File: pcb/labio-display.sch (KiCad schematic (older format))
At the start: 6 parts, among them P401 SFV12R-1ST__HLF, SW401 DIP_SWITCH_X04, U401 CFAL12832D-B

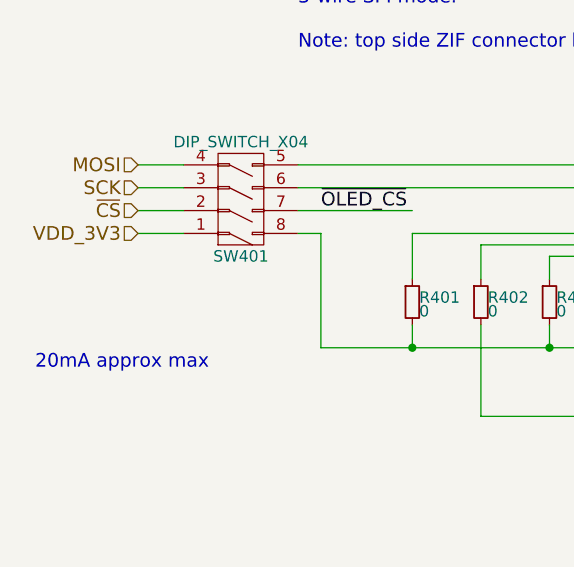
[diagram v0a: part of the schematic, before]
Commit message: Fix ADC reading mic, possible backpowering, encoder pull downs, vias in footprint:
* Mic needs on-board path to ADC. Add proper bias and amp. Connect to ADC or codec with switches.
* Mic footprint (U701) flipped. Redraw footprint and adjust routing.
* Remove power from dip switches and replace with fuses. Turning power off to a block could result in backpower from driven IO lines.
* Remove/adjust pull downs on LEDs for encoder/dpad lines.
* Move vias out of display connector (P401) footprint.
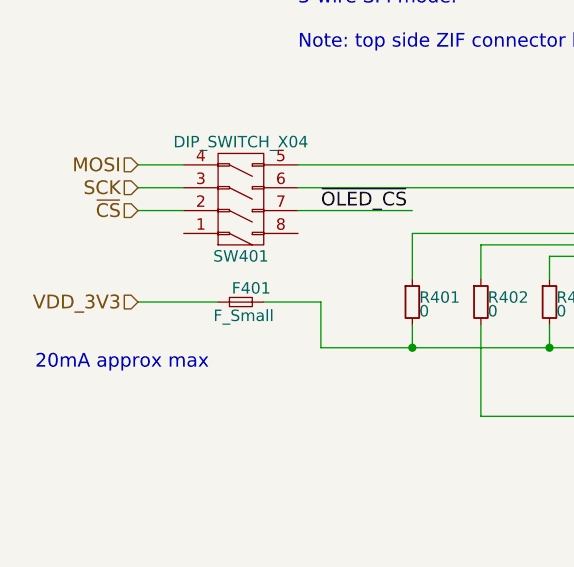
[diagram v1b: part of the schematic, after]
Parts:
- added F401: F_Small, Resistors_SMD:R_1206, symbol F_Small
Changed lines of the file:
@@
 encoding utf-8
 Sheet 4 10
-Title ""
+Title "Raspberry Pi Embedded Lab I/O"
 Date ""
-Rev ""
-Comp ""
+Rev "1.1.4"
+Comp "Carnegie Mellon University"
 Comment1 ""
-Comment2 ""
+Comment2 "Drawn by: Ian Hartwig"
 Comment3 ""
 Comment4 ""
@@
 	6000 2400 6600 2400
 Connection ~ 6000 3500
-Text HLabel 3800 2900 0    60   Input ~ 0
+Text HLabel 3800 3200 0    60   Input ~ 0
 VDD_3V3
 Text HLabel 3800 2800 0    60   Input ~ 0
@@
 03 00 00 00 00 F4 24 84 F2 00 00 00 00 00 3D 09 A1 3C 00 00 00 00 40 4F 42 28 0F 00 00 00 00 D0
 93 10 CA 03 00 00 00 00 F4 24 84 F2 00 00 00 00 00 3D 09 A1 3C 00 00 00 00 40 4F FA 3F 4E 16 A4
-A2 80 4C E9 AA 00 00 00 00 49 45 4E 44 AE 42 60 82 00
+A2 80 4C E9 AA 00 00 00 00 49 45 4E 44 AE 42 60 82 3B
 EndData
 $EndBitmap
@@
 $EndComp
 Wire Wire Line
-	3800 2900 4000 2900
-Wire Wire Line
 	4000 2600 3800 2600
 Wire Wire Line
@@
 	4600 3400 6600 3400
 Wire Wire Line
-	4600 3400 4600 2900
-Wire Wire Line
-	4600 2900 4500 2900
-Wire Wire Line
 	6600 3300 6100 3300
 Wire Wire Line
@@
 	1    0    0    -1
 $EndComp
+$Comp
+L F_Small F401
+U 1 1 57AFAD90
+P 4250 3200
+F 0 "F401" H 4210 3260 50  0000 L CNN
+F 1 "F_Small" H 4130 3140 50  0000 L CNN
+F 2 "Resistors_SMD:R_1206" H 4250 3200 50  0001 C CNN
+F 3 "" H 4250 3200 50  0000 C CNN
+	1    4250 3200
+	1    0    0    -1
+$EndComp
+Wire Wire Line
+	4350 3200 4600 3200
+Wire Wire Line
+	4600 3200 4600 3400
+Wire Wire Line
+	3800 3200 4150 3200
 $EndSCHEMATC

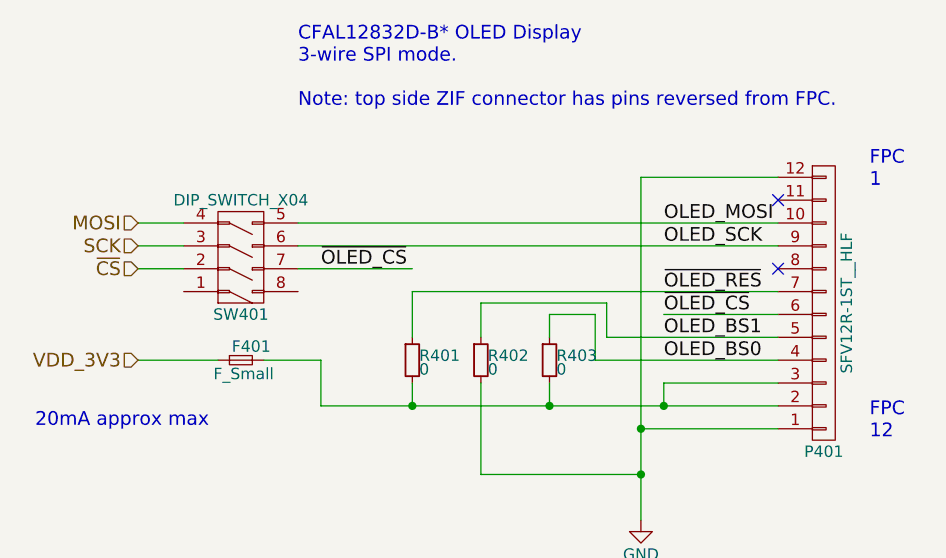
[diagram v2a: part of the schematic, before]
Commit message: using MISO/gpio for D/C on led screen and layout. bump to rev 1.2.0.
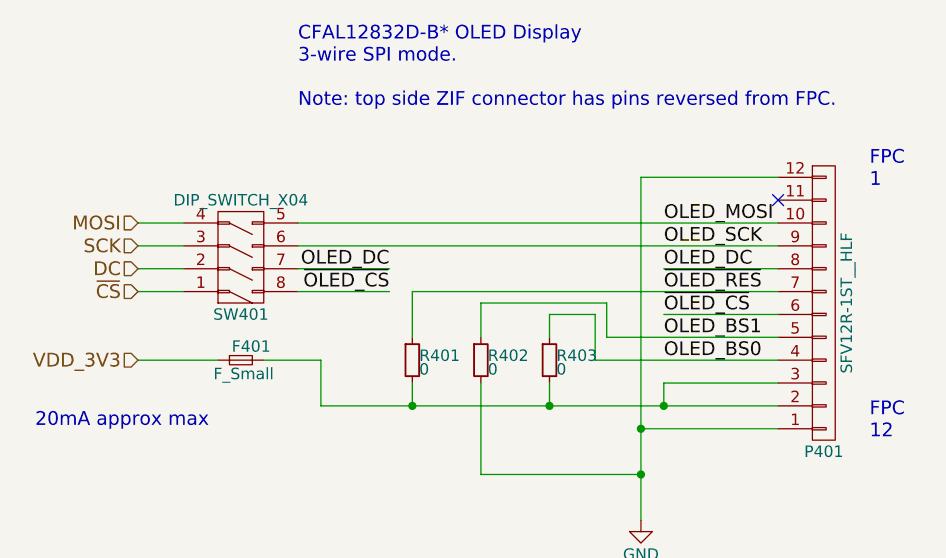
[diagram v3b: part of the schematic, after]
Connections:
- net labels added: DC, OLED_DC
- wire segments 30 -> 33
- no-connect marks 2 -> 1
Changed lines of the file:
@@
 Title "Raspberry Pi Embedded Lab I/O"
 Date ""
-Rev "1.1.4"
+Rev "1.2.0"
 Comp "Carnegie Mellon University"
 Comment1 ""
@@
 Text HLabel 3800 3200 0    60   Input ~ 0
 VDD_3V3
-Text HLabel 3800 2800 0    60   Input ~ 0
+Text HLabel 3800 2900 0    60   Input ~ 0
 ~CS
-NoConn ~ 6600 2800
 Text HLabel 3800 2700 0    60   Input ~ 0
 SCK
@@
 03 00 00 00 00 F4 24 84 F2 00 00 00 00 00 3D 09 A1 3C 00 00 00 00 40 4F 42 28 0F 00 00 00 00 D0
 93 10 CA 03 00 00 00 00 F4 24 84 F2 00 00 00 00 00 3D 09 A1 3C 00 00 00 00 40 4F FA 3F 4E 16 A4
-A2 80 4C E9 AA 00 00 00 00 49 45 4E 44 AE 42 60 82 A3
+A2 80 4C E9 AA 00 00 00 00 49 45 4E 44 AE 42 60 82 FF
 EndData
 $EndBitmap
@@
 Text Label 6100 3000 0    60   ~ 0
 ~OLED_CS
-Text Label 4600 2800 0    60   ~ 0
+Text Label 4900 2900 2    60   ~ 0
 ~OLED_CS
 Wire Wire Line
-	4500 2800 5000 2800
+	4500 2800 4900 2800
 Text Label 6100 2700 0    60   ~ 0
 OLED_SCK
@@
 Wire Wire Line
 	3800 3200 4150 3200
+Wire Wire Line
+	6600 2800 6100 2800
+Text Label 6100 2800 0    60   ~ 0
+OLED_DC
+Wire Wire Line
+	4500 2900 4900 2900
+Text Label 4900 2800 2    60   ~ 0
+OLED_DC
+Text HLabel 3800 2800 0    60   Input ~ 0
+DC
+Wire Wire Line
+	3800 2900 4000 2900
 $EndSCHEMATC

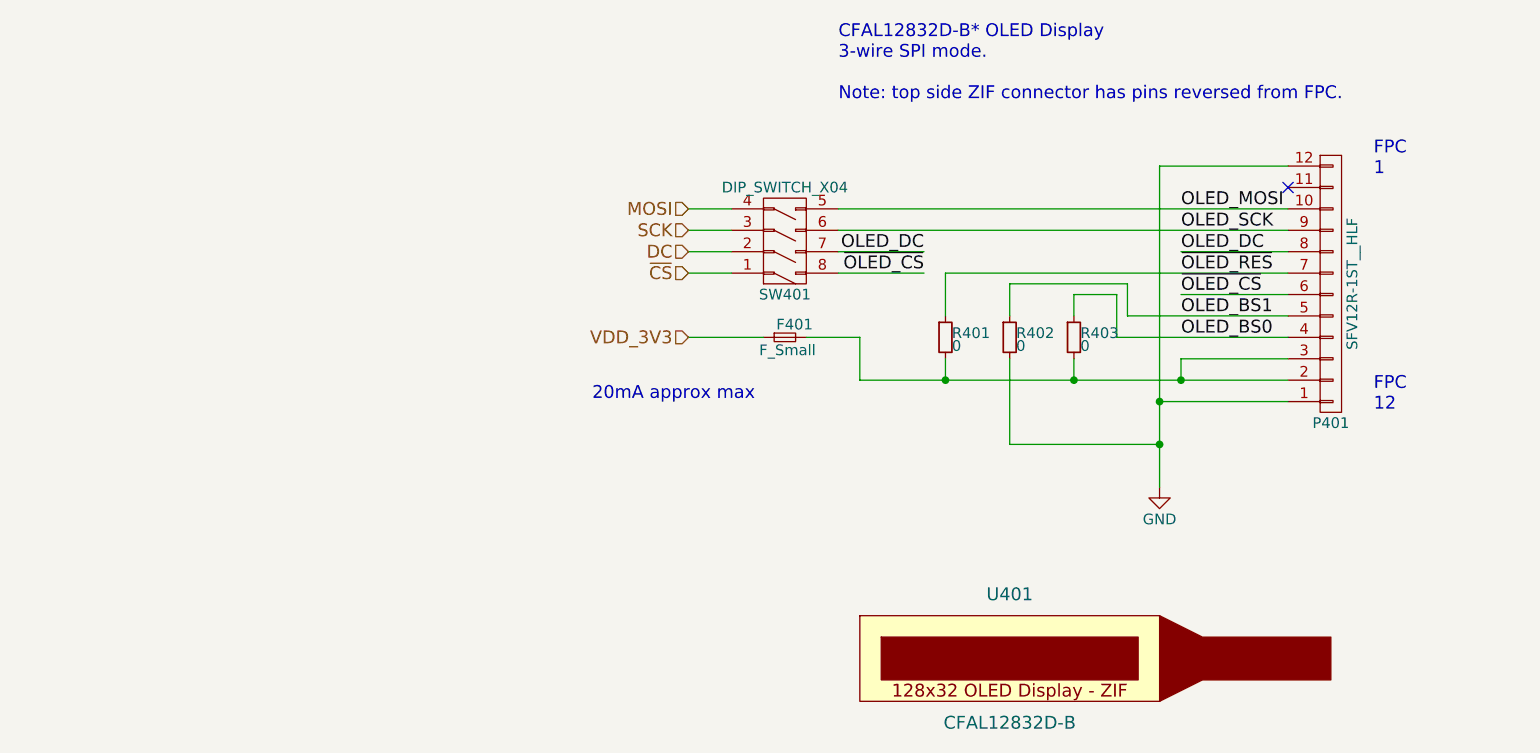
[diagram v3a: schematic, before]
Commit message: add options for driving oled reset. no changes to stuffed bom parts.
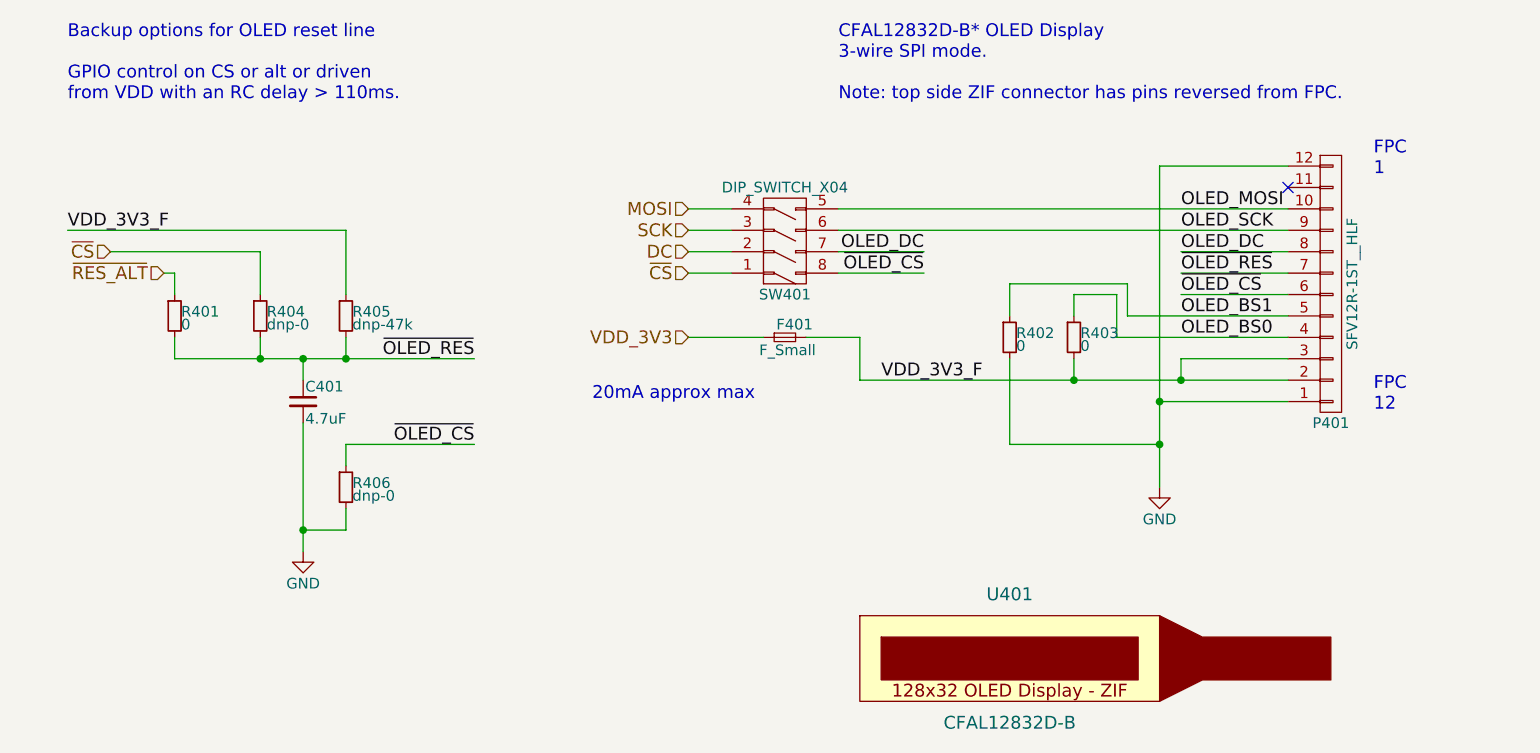
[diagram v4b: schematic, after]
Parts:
- added C401: 4.7uF, Capacitors_SMD:C_0805, symbol C_Small
- added R401: 0, Resistors_SMD:R_0603, symbol R_Small
- added R404, R406: dnp-0, Resistors_SMD:R_0603, symbol R_Small
- R405: renamed from R401; value 0 -> dnp-47k
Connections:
- net GND: now also C401.2, R406.2
- net ~CS: now also R404.1
- net ~OLED_CS: now also R406.1
- net ~OLED_RES: now also R405.2, C401.1, R401.2, R404.2; no longer R405.1
- net VDD_3V3_F: now reaches F401.2, P401.2 (P2), P401.3 (P3), R403.2
- net VDD_3V3_F: now also R405.1; no longer R405.2
- new net ~RES_ALT: R401.1
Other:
- note added: "Backup options for OLED reset line\n\nGPIO control on CS or alt or driven\nfrom VDD with an RC delay > 110ms."
- moved on the sheet: R405
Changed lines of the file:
@@
 20mA approx max
 $Comp
-L R_Small R401
+L R_Small R405
 U 1 1 5766D812
-P 5000 3200
-F 0 "R401" H 5030 3220 50  0000 L CNN
-F 1 "0" H 5030 3160 50  0000 L CNN
-F 2 "Resistors_SMD:R_0603" H 5000 3200 50  0001 C CNN
-F 3 "" H 5000 3200 50  0000 C CNN
-	1    5000 3200
+P 2200 3100
+F 0 "R405" H 2230 3120 50  0000 L CNN
+F 1 "dnp-47k" H 2230 3060 50  0000 L CNN
+F 2 "Resistors_SMD:R_0603" H 2200 3100 50  0001 C CNN
+F 3 "" H 2200 3100 50  0000 C CNN
+	1    2200 3100
 	1    0    0    -1
 $EndComp
@@
 	5600 3300 5600 3400
 Connection ~ 5600 3400
-Wire Wire Line
-	5000 3300 5000 3400
-Connection ~ 5000 3400
-Wire Wire Line
-	6600 2900 5000 2900
-Wire Wire Line
-	5000 2900 5000 3100
 $Comp
 L R_Small R402
@@
 Wire Wire Line
 	3800 2900 4000 2900
+$Comp
+L C_Small C401
+U 1 1 57BD0C4A
+P 2000 3500
+F 0 "C401" H 2010 3570 50  0000 L CNN
+F 1 "4.7uF" H 2010 3420 50  0000 L CNN
+F 2 "Capacitors_SMD:C_0805" H 2000 3500 50  0001 C CNN
+F 3 "" H 2000 3500 50  0000 C CNN
+	1    2000 3500
+	1    0    0    -1
+$EndComp
+$Comp
+L R_Small R404
+U 1 1 57BD0DE0
+P 1800 3100
+F 0 "R404" H 1830 3120 50  0000 L CNN
+F 1 "dnp-0" H 1830 3060 50  0000 L CNN
+F 2 "Resistors_SMD:R_0603" H 1800 3100 50  0001 C CNN
+F 3 "" H 1800 3100 50  0000 C CNN
+	1    1800 3100
+	1    0    0    -1
+$EndComp
+$Comp
+L R_Small R401
+U 1 1 57BD0E72
+P 1400 3100
+F 0 "R401" H 1430 3120 50  0000 L CNN
+F 1 "0" H 1430 3060 50  0000 L CNN
+F 2 "Resistors_SMD:R_0603" H 1400 3100 50  0001 C CNN
+F 3 "" H 1400 3100 50  0000 C CNN
+	1    1400 3100
+	1    0    0    -1
+$EndComp
+$Comp
+L R_Small R406
+U 1 1 57BD0EA6
+P 2200 3900
+F 0 "R406" H 2230 3920 50  0000 L CNN
+F 1 "dnp-0" H 2230 3860 50  0000 L CNN
+F 2 "Resistors_SMD:R_0603" H 2200 3900 50  0001 C CNN
+F 3 "" H 2200 3900 50  0000 C CNN
+	1    2200 3900
+	1    0    0    -1
+$EndComp
+Wire Wire Line
+	6600 2900 6100 2900
+Wire Wire Line
+	1400 3000 1400 2900
+Wire Wire Line
+	1400 2900 1350 2900
+$Comp
+L GND #PWR010
+U 1 1 57BD11F8
+P 2000 4200
+F 0 "#PWR010" H 2000 3950 50  0001 C CNN
+F 1 "GND" H 2000 4050 50  0000 C CNN
+F 2 "" H 2000 4200 50  0000 C CNN
+F 3 "" H 2000 4200 50  0000 C CNN
+	1    2000 4200
+	1    0    0    -1
+$EndComp
+Wire Wire Line
+	2000 4200 2000 3600
+Wire Wire Line
+	1400 3200 1400 3300
+Wire Wire Line
+	1400 3300 2800 3300
+Wire Wire Line
+	2000 3300 2000 3400
+Wire Wire Line
+	1800 3300 1800 3200
+Connection ~ 1800 3300
+Connection ~ 2000 3300
+Wire Wire Line
+	2200 3200 2200 3300
+Connection ~ 2200 3300
+Wire Wire Line
+	1800 3000 1800 2800
+Wire Wire Line
+	1800 2800 1100 2800
+Wire Wire Line
+	2200 3000 2200 2700
+Wire Wire Line
+	2200 2700 900  2700
+Text Label 4700 3400 0    60   ~ 0
+VDD_3V3_F
+Text Label 900  2700 0    60   ~ 0
+VDD_3V3_F
+Text Label 2800 3300 2    60   ~ 0
+~OLED_RES
+Wire Wire Line
+	2200 3700 2800 3700
+Text Label 2800 3700 2    60   ~ 0
+~OLED_CS
+Text HLabel 1100 2800 0    60   Input ~ 0
+~CS
+Text HLabel 1350 2900 0    60   Input ~ 0
+~RES_ALT
+Wire Wire Line
+	2200 3700 2200 3800
+Wire Wire Line
+	2200 4000 2200 4100
+Wire Wire Line
+	2200 4100 2000 4100
+Connection ~ 2000 4100
+Text Notes 900  2100 0    60   ~ 0
+Backup options for OLED reset line\n\nGPIO control on CS or alt or driven\nfrom VDD with an RC delay > 110ms.
 $EndSCHEMATC

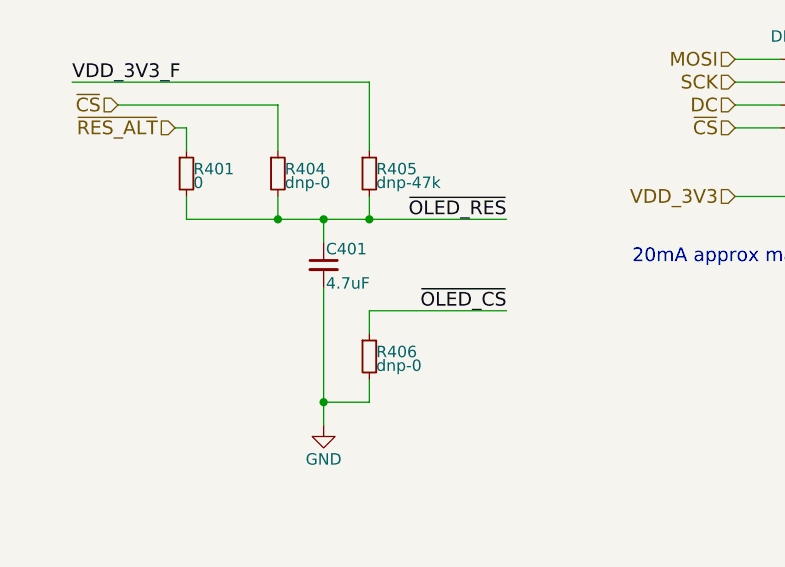
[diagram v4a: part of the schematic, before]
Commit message: add through hole parts to the bom (highlighted). update schematic pdf.
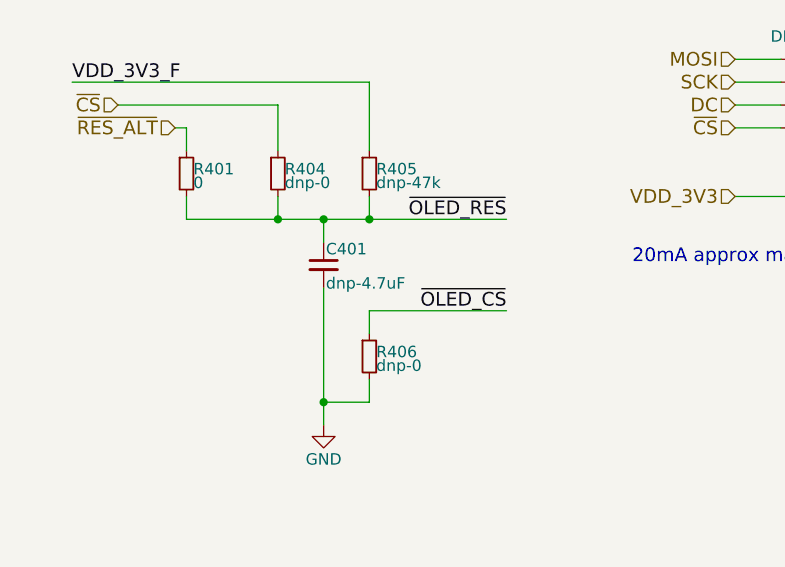
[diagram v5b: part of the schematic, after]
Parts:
- C401: value 4.7uF -> dnp-4.7uF
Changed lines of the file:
@@
 03 00 00 00 00 F4 24 84 F2 00 00 00 00 00 3D 09 A1 3C 00 00 00 00 40 4F 42 28 0F 00 00 00 00 D0
 93 10 CA 03 00 00 00 00 F4 24 84 F2 00 00 00 00 00 3D 09 A1 3C 00 00 00 00 40 4F FA 3F 4E 16 A4
-A2 80 4C E9 AA 00 00 00 00 49 45 4E 44 AE 42 60 82 FF
+A2 80 4C E9 AA 00 00 00 00 49 45 4E 44 AE 42 60 82 00
 EndData
 $EndBitmap
@@
 P 2000 3500
 F 0 "C401" H 2010 3570 50  0000 L CNN
-F 1 "4.7uF" H 2010 3420 50  0000 L CNN
+F 1 "dnp-4.7uF" H 2010 3420 50  0000 L CNN
 F 2 "Capacitors_SMD:C_0805" H 2000 3500 50  0001 C CNN
 F 3 "" H 2000 3500 50  0000 C CNN
